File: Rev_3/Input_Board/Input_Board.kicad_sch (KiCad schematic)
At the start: 7 parts, among them J1 6, J2 6, J3 6

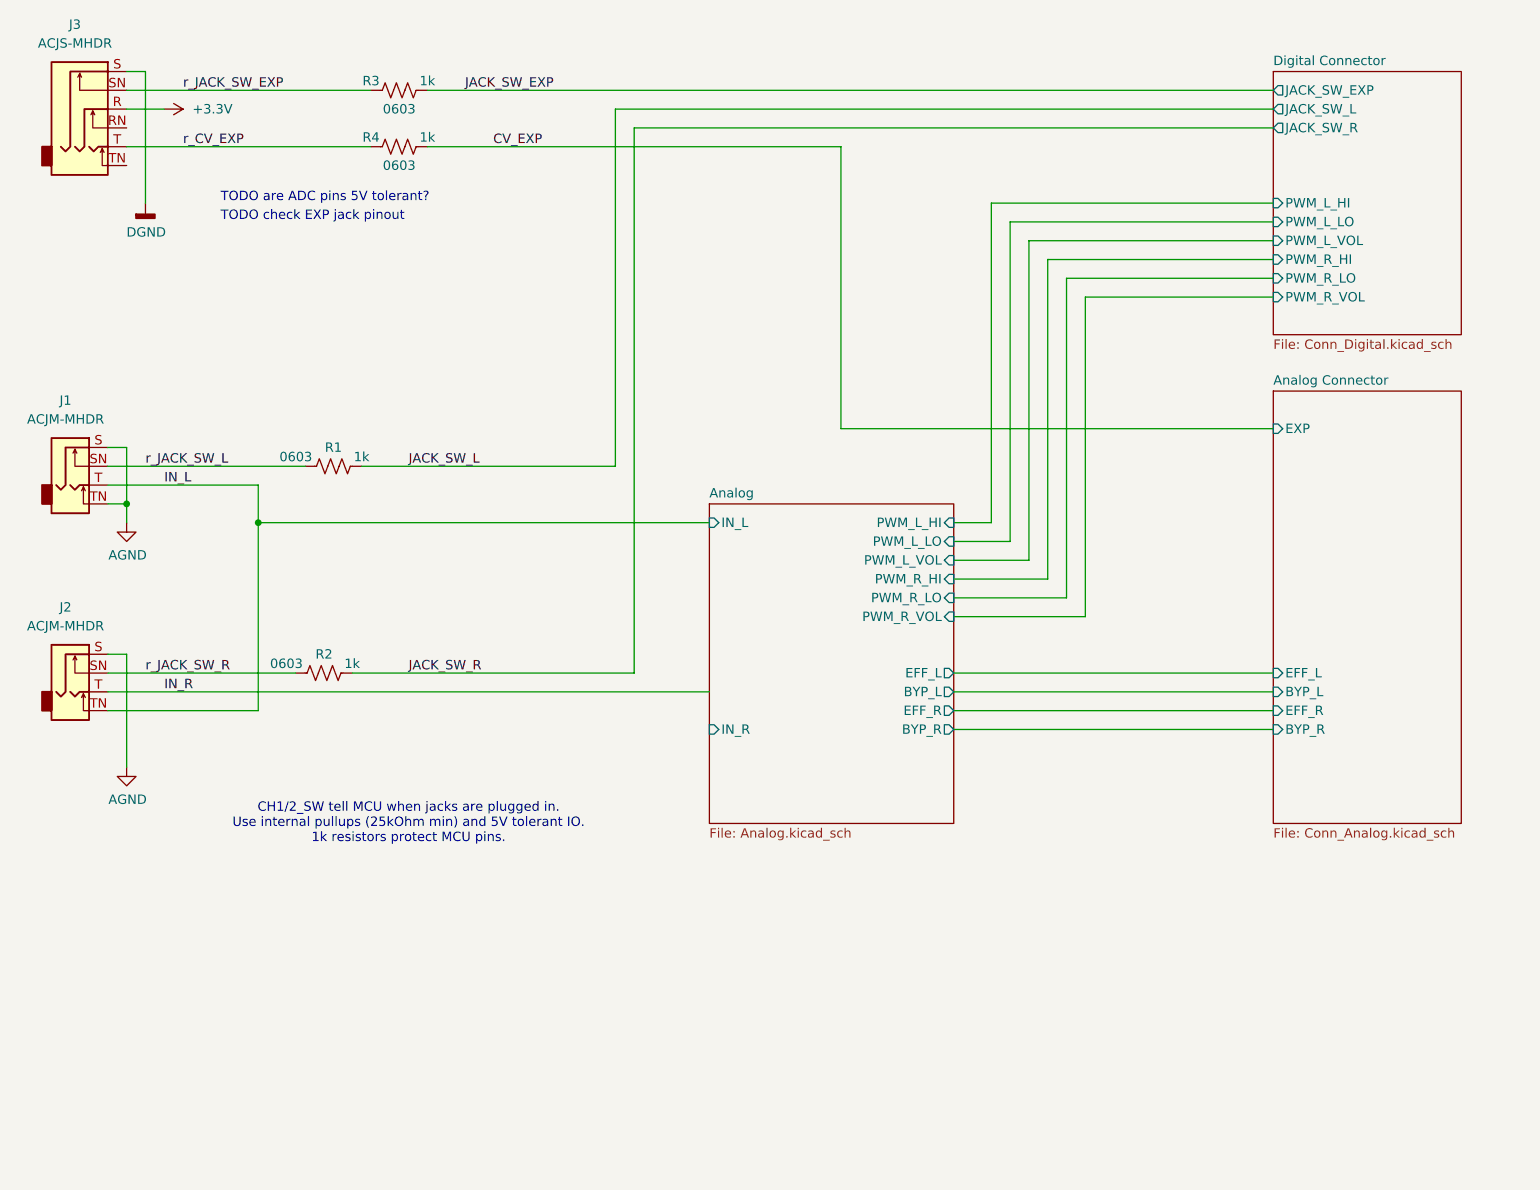
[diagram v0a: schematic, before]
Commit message: Added analog board back, switched to Jacks on Bottom
Added analog board mezzanine back to fit everything. Finalized decision on jack boards; jacks on bottom, wire to board connectors between jack boards and digital board. Tentative board outlines defined and scoped out component placement.
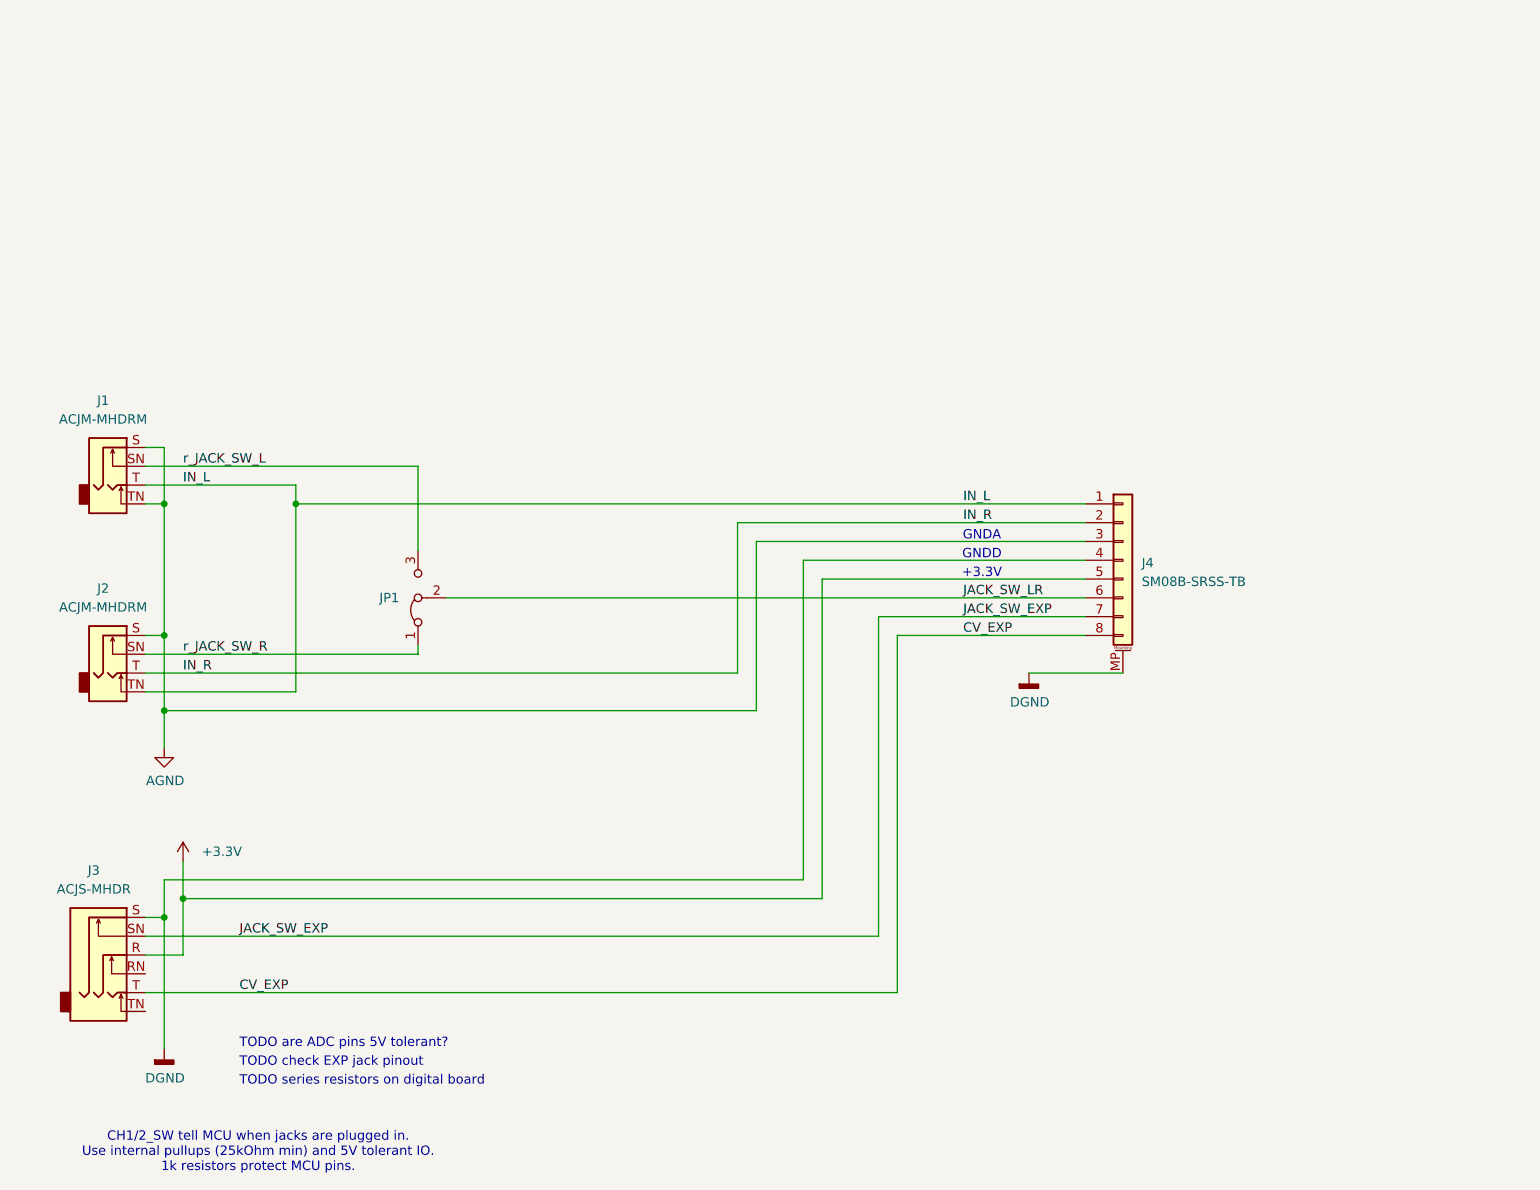
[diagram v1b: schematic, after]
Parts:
- removed R1, R2, R3, R4: 1k, Resistor_SMD:R_0603_1608Metric, symbol #gplm:res/RES-2001-001K
- added J4: 8, Connector_JST:JST_SH_BM08B-SRSS-TB_1x08-1MP_P1.00mm_Vertical, symbol #gplm:con/CON-5001-0008
- added JP1: Jumper_3_Bridged12, Jumper:SolderJumper-3_P1.3mm_Bridged12_Pad1.0x1.5mm, symbol #gplm:art/ART-1000-0003
- J1, J2: symbol #gplm:con/CON-1003-M300 -> #gplm:con/CON-1003-M301; IPN CON-1003-M300 -> CON-1003-M301; MPN ACJM-MHDR -> ACJM-MHDRM; Pins 6 -> 4
- J3: Manufacturer Neutrik -> Amphenol Audio; Pins 6 -> 4
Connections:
- net r_CV_EXP is gone; now on net CV_EXP: J3.T
- net r_JACK_SW_EXP is gone; now on net JACK_SW_EXP: J3.SN
- net +3.3V: now also J4.5 (Pin_5)
- net AGND: now also J4.3 (Pin_3)
- net CV_EXP: now also J4.8 (Pin_8)
- net DGND: now also J4.4 (Pin_4), J4.MP (MountPin)
- net IN_L: now also J4.1 (Pin_1)
- net IN_R: now also J4.2 (Pin_2)
- net JACK_SW_EXP: now also J4.7 (Pin_7)
- net r_JACK_SW_L: now also JP1.3 (B)
- net r_JACK_SW_R: now also JP1.1 (A)
- new net JACK_SW_LR: J4.6 (Pin_6), JP1.2 (C)
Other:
- removed sheet Analog
- removed sheet Analog Connector
- removed sheet Digital Connector
- note added: "+3.3V"
- note added: "GNDA"
- note added: "GNDD"
- note added: "TODO series resistors on digital board"
- moved on the sheet: J1, J2, J3
